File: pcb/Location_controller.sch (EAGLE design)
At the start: 50 parts, among them IC1 LIS302DL

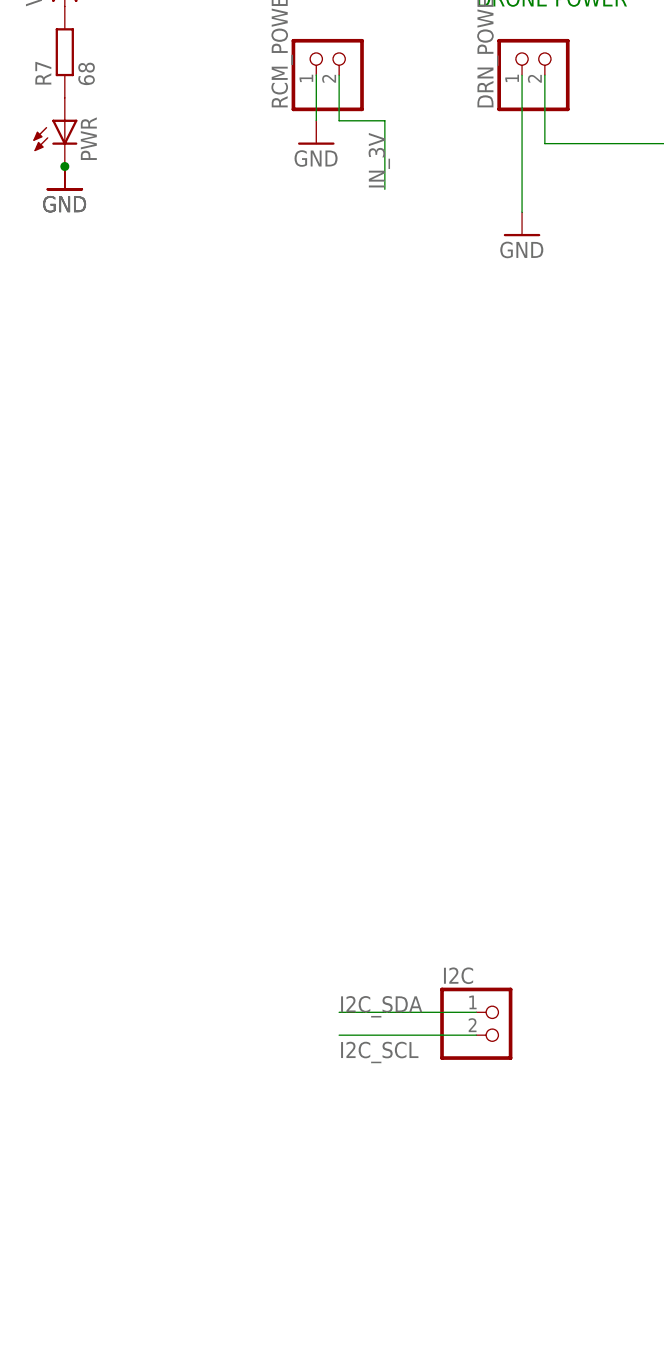
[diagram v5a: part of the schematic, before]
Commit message: Add Zener Diodes to I2C pins
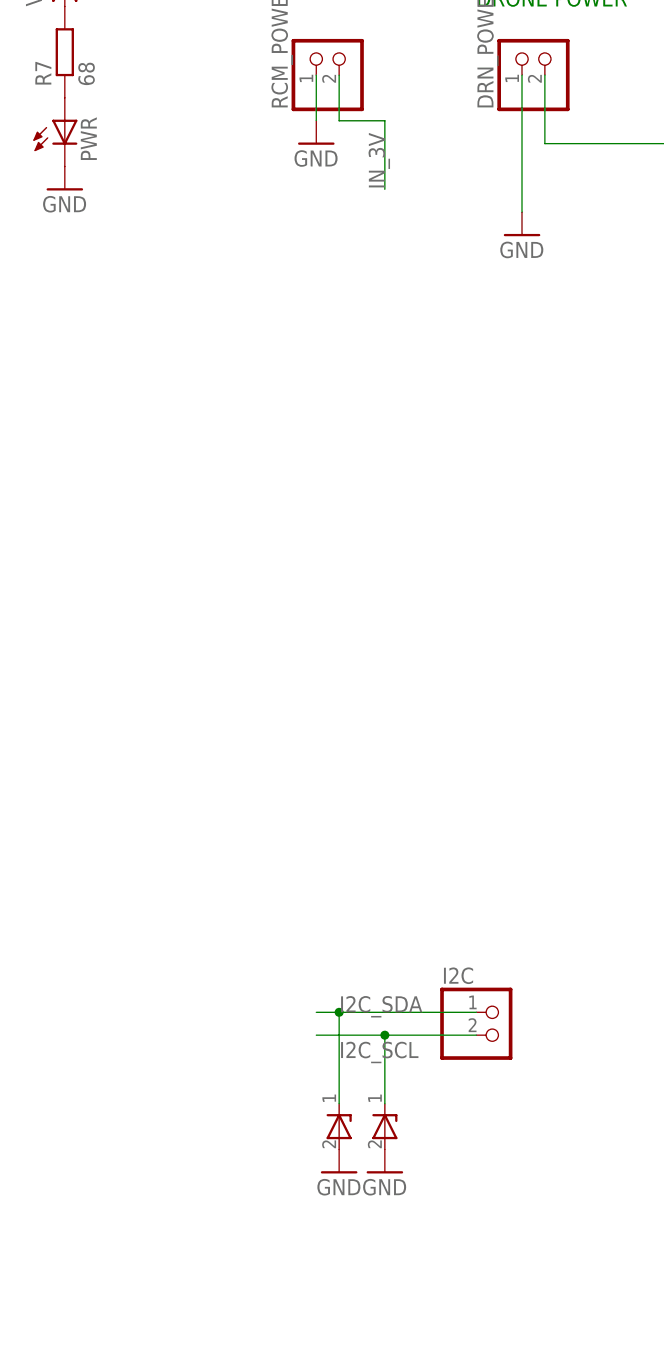
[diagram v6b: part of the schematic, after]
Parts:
- added D1, D2: ZDIODE, stm32f4:ZDIODE
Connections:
- net GND: now also D1.P2, D2.P2
- net I2C_SCL: now also D2.P1
- net I2C_SDA: now also D1.P1
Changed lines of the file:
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@@
 <part name="R8" library="eagle-ltspice" deviceset="R" device="" value="68"/>
 <part name="ERR" library="eagle-ltspice" deviceset="LED_E" device=""/>
-<part name="GND21" library="supply1" deviceset="GND" device=""/>
 <part name="GND22" library="supply1" deviceset="GND" device=""/>
 <part name="I2C" library="pinhead" deviceset="PINHD-1X2" device=""/>
+<part name="D1" library="stm32f4" deviceset="ZDIODE" device=""/>
+<part name="D2" library="stm32f4" deviceset="ZDIODE" device=""/>
+<part name="GND23" library="supply1" deviceset="GND" device=""/>
+<part name="GND24" library="supply1" deviceset="GND" device=""/>
 </parts>
 <sheets>
@@
 <instance part="R8" gate="G$1" x="147.32" y="48.26" rot="R90"/>
 <instance part="ERR" gate="G$1" x="147.32" y="38.1"/>
-<instance part="GND21" gate="1" x="-154.94" y="106.68"/>
 <instance part="GND22" gate="1" x="147.32" y="27.94"/>
 <instance part="I2C" gate="G$1" x="-106.68" y="12.7"/>
+<instance part="D1" gate="G$1" x="-124.46" y="2.54" rot="R90"/>
+<instance part="D2" gate="G$1" x="-119.38" y="2.54" rot="R90"/>
+<instance part="GND23" gate="1" x="-124.46" y="-2.54"/>
+<instance part="GND24" gate="1" x="-119.38" y="-2.54"/>
 </instances>
 <busses>
@@
 <pinref part="PWR" gate="G$1" pin="C"/>
 <pinref part="GND20" gate="1" pin="GND"/>
-<pinref part="GND21" gate="1" pin="GND"/>
-<junction x="-154.94" y="109.22"/>
-<pinref part="GND21" gate="1" pin="GND"/>
 </segment>
 <segment>
@@
 <pinref part="ERR" gate="G$1" pin="C"/>
 <wire x1="147.32" y1="30.48" x2="147.32" y2="33.02" width="0.1524" layer="91"/>
+</segment>
+<segment>
+<pinref part="D1" gate="G$1" pin="P2"/>
+<pinref part="GND23" gate="1" pin="GND"/>
+</segment>
+<segment>
+<pinref part="D2" gate="G$1" pin="P2"/>
+<pinref part="GND24" gate="1" pin="GND"/>
 </segment>
 </net>
@@
 <segment>
 <pinref part="I2C" gate="G$1" pin="2"/>
-<wire x1="-109.22" y1="12.7" x2="-124.46" y2="12.7" width="0.1524" layer="91"/>
+<wire x1="-109.22" y1="12.7" x2="-119.38" y2="12.7" width="0.1524" layer="91"/>
 <label x="-124.46" y="10.16" size="1.778" layer="95"/>
+<pinref part="D2" gate="G$1" pin="P1"/>
+<wire x1="-119.38" y1="12.7" x2="-127" y2="12.7" width="0.1524" layer="91"/>
+<wire x1="-119.38" y1="5.08" x2="-119.38" y2="12.7" width="0.1524" layer="91"/>
+<junction x="-119.38" y="12.7"/>
 </segment>
 </net>
@@
 <wire x1="-109.22" y1="15.24" x2="-124.46" y2="15.24" width="0.1524" layer="91"/>
 <label x="-124.46" y="15.24" size="1.778" layer="95"/>
-</segment>
-</net>
+<pinref part="D1" gate="G$1" pin="P1"/>
+<wire x1="-124.46" y1="15.24" x2="-127" y2="15.24" width="0.1524" layer="91"/>
+<wire x1="-124.46" y1="5.08" x2="-124.46" y2="15.24" width="0.1524" layer="91"/>
+<junction x="-124.46" y="15.24"/>
+</segment>
+</net>

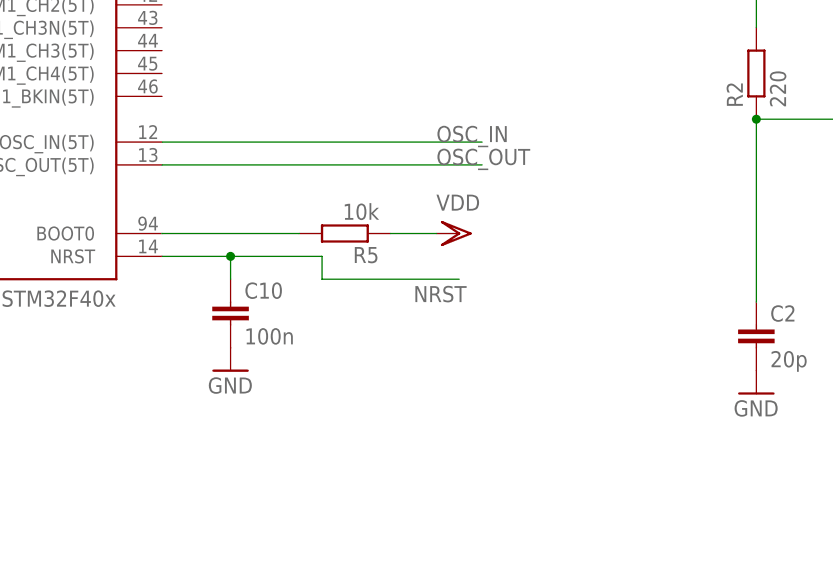
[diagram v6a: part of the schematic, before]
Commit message: Add resistor to GND at BOOT0
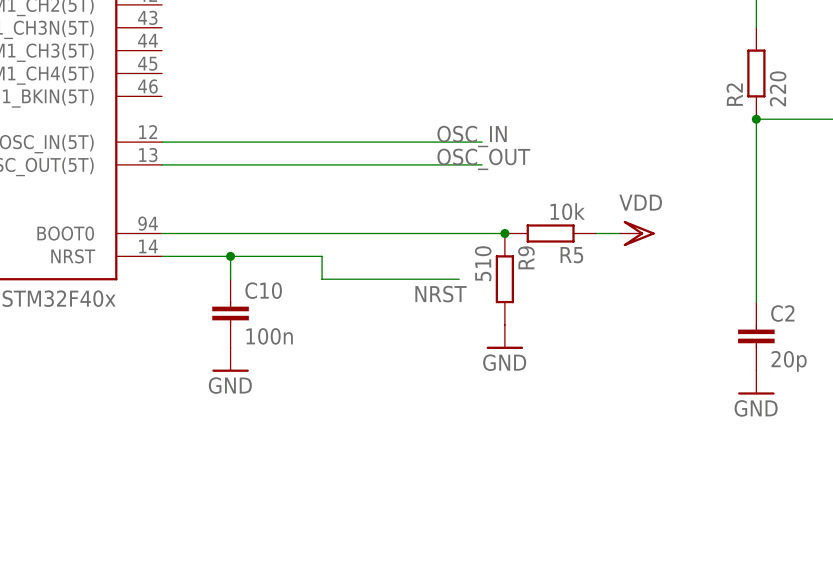
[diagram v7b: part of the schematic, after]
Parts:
- added R9: 510, eagle-ltspice:R
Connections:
- net GND: now also R9.2
- net N$3: now also R9.1
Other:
- moved on the sheet: R5
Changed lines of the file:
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@@
 <part name="GND23" library="supply1" deviceset="GND" device=""/>
 <part name="GND24" library="supply1" deviceset="GND" device=""/>
+<part name="R9" library="eagle-ltspice" deviceset="R" device="" value="510"/>
+<part name="GND21" library="supply1" deviceset="GND" device=""/>
 </parts>
 <sheets>
@@
 <instance part="POWER" gate="A" x="-78.74" y="99.06" rot="R270"/>
 <instance part="GND7" gate="1" x="-40.64" y="-81.28"/>
-<instance part="VDD2" gate="G$1" x="152.4" y="-7.62" rot="R270"/>
-<instance part="R5" gate="G$1" x="139.7" y="-7.62" rot="R180"/>
+<instance part="VDD2" gate="G$1" x="172.72" y="-7.62" rot="R270"/>
+<instance part="R5" gate="G$1" x="162.56" y="-7.62" rot="R180"/>
 <instance part="VDD8" gate="G$1" x="40.64" y="147.32"/>
 <instance part="C26" gate="G$1" x="238.76" y="93.98"/>
@@
 <instance part="GND23" gate="1" x="-124.46" y="-2.54"/>
 <instance part="GND24" gate="1" x="-119.38" y="-2.54"/>
+<instance part="R9" gate="G$1" x="157.48" y="-12.7" rot="R270"/>
+<instance part="GND21" gate="1" x="157.48" y="-20.32"/>
 </instances>
 <busses>
@@
 <pinref part="GND24" gate="1" pin="GND"/>
 </segment>
+<segment>
+<pinref part="R9" gate="G$1" pin="2"/>
+<pinref part="GND21" gate="1" pin="GND"/>
+</segment>
 </net>
 <net name="N$1" class="0">
@@
 </segment>
 <segment>
-<pinref part="R5" gate="G$1" pin="1"/>
-<pinref part="VDD2" gate="G$1" pin="VDD"/>
-<wire x1="144.78" y1="-7.62" x2="149.86" y2="-7.62" width="0.1524" layer="91"/>
-</segment>
-<segment>
 <pinref part="U$1" gate="G$1" pin="VBAT"/>
 <pinref part="VDD8" gate="G$1" pin="VDD"/>
@@
 <pinref part="VDD10" gate="G$1" pin="VDD"/>
 </segment>
+<segment>
+<pinref part="R5" gate="G$1" pin="1"/>
+<pinref part="VDD2" gate="G$1" pin="VDD"/>
+<wire x1="167.64" y1="-7.62" x2="170.18" y2="-7.62" width="0.1524" layer="91"/>
+</segment>
 </net>
 <net name="I2C_SCL" class="0">
@@
 <wire x1="-30.48" y1="-63.5" x2="-30.48" y2="-78.74" width="0.1524" layer="91"/>
 <label x="-30.48" y="-78.74" size="1.778" layer="95" rot="R90"/>
-</segment>
-</net>
-<net name="N$3" class="0">
-<segment>
-<pinref part="R5" gate="G$1" pin="2"/>
-<pinref part="U$1" gate="G$1" pin="BOOT0"/>
-<wire x1="134.62" y1="-7.62" x2="119.38" y2="-7.62" width="0.1524" layer="91"/>
 </segment>
 </net>
@@
 </segment>
 </net>
+<net name="N$3" class="0">
+<segment>
+<pinref part="R5" gate="G$1" pin="2"/>
+<pinref part="R9" gate="G$1" pin="1"/>
+<pinref part="U$1" gate="G$1" pin="BOOT0"/>
+<wire x1="157.48" y1="-7.62" x2="119.38" y2="-7.62" width="0.1524" layer="91"/>
+<junction x="157.48" y="-7.62"/>
+</segment>
+</net>

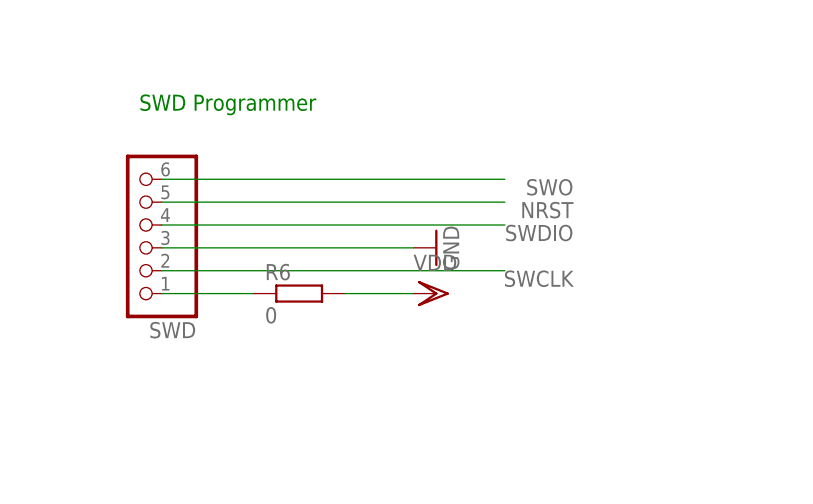
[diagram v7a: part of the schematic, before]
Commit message: added zener to SWDIO EN SWO
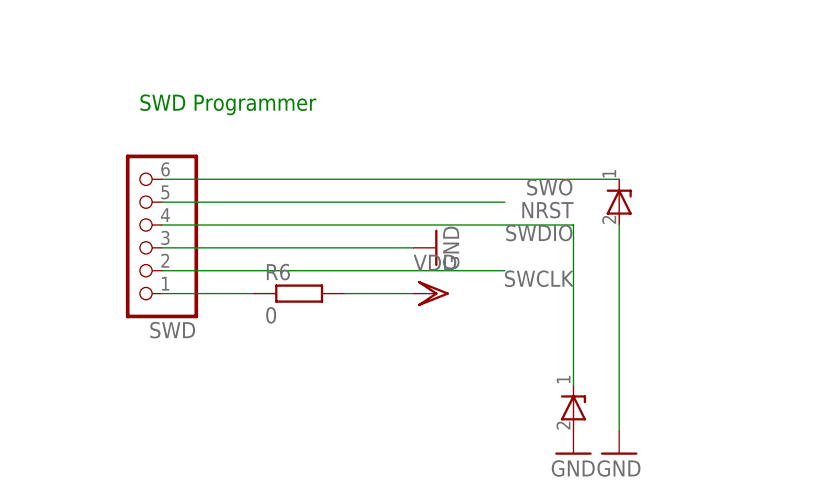
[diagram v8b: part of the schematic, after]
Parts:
- added D3, D4: ZDIODE, stm32f4:ZDIODE
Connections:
- net GND: now also D3.P2, D4.P2
- net SWDIO: now also D4.P1
- net SWO: now also D3.P1
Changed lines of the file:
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@@
 <?xml version="1.0" encoding="utf-8"?>
 <!DOCTYPE eagle SYSTEM "eagle.dtd">
-<eagle version="6.5.0">
+<eagle version="6.4">
 <drawing>
 <settings>
@@
 <part name="R9" library="eagle-ltspice" deviceset="R" device="" value="510"/>
 <part name="GND21" library="supply1" deviceset="GND" device=""/>
+<part name="D4" library="stm32f4" deviceset="ZDIODE" device=""/>
+<part name="GND26" library="supply1" deviceset="GND" device=""/>
+<part name="D3" library="stm32f4" deviceset="ZDIODE" device=""/>
+<part name="GND25" library="supply1" deviceset="GND" device=""/>
 </parts>
 <sheets>
@@
 <instance part="R9" gate="G$1" x="157.48" y="-12.7" rot="R270"/>
 <instance part="GND21" gate="1" x="157.48" y="-20.32"/>
+<instance part="D4" gate="G$1" x="73.66" y="-83.82" rot="R90"/>
+<instance part="GND26" gate="1" x="73.66" y="-88.9"/>
+<instance part="D3" gate="G$1" x="78.74" y="-60.96" rot="R90"/>
+<instance part="GND25" gate="1" x="78.74" y="-88.9"/>
 </instances>
 <busses>
@@
 <pinref part="GND21" gate="1" pin="GND"/>
 </segment>
+<segment>
+<pinref part="D4" gate="G$1" pin="P2"/>
+<pinref part="GND26" gate="1" pin="GND"/>
+</segment>
+<segment>
+<pinref part="D3" gate="G$1" pin="P2"/>
+<pinref part="GND25" gate="1" pin="GND"/>
+<wire x1="78.74" y1="-86.36" x2="78.74" y2="-63.5" width="0.1524" layer="91"/>
+</segment>
 </net>
 <net name="N$1" class="0">
@@
 <segment>
 <pinref part="SWD" gate="A" pin="6"/>
-<wire x1="27.94" y1="-58.42" x2="66.04" y2="-58.42" width="0.1524" layer="91"/>
+<wire x1="27.94" y1="-58.42" x2="78.74" y2="-58.42" width="0.1524" layer="91"/>
 <label x="73.66" y="-58.42" size="1.778" layer="95" rot="R180"/>
+<pinref part="D3" gate="G$1" pin="P1"/>
 </segment>
 <segment>
@@
 <net name="SWDIO" class="0">
 <segment>
-<pinref part="SWD" gate="A" pin="4"/>
-<wire x1="27.94" y1="-63.5" x2="66.04" y2="-63.5" width="0.1524" layer="91"/>
-<label x="73.66" y="-63.5" size="1.778" layer="95" rot="R180"/>
-</segment>
-<segment>
 <pinref part="U$1" gate="G$1" pin="PA13/JTMS-SWDAT(5T)"/>
 <wire x1="40.64" y1="38.1" x2="22.86" y2="38.1" width="0.1524" layer="91"/>
 <label x="22.86" y="38.1" size="1.778" layer="95"/>
 </segment>
-</net>
+<segment>
+<pinref part="SWD" gate="A" pin="4"/>
+<wire x1="27.94" y1="-63.5" x2="73.66" y2="-63.5" width="0.1524" layer="91"/>
+<label x="73.66" y="-63.5" size="1.778" layer="95" rot="R180"/>
+<wire x1="73.66" y1="-63.5" x2="73.66" y2="-81.28" width="0.1524" layer="91"/>
+<pinref part="D4" gate="G$1" pin="P1"/>
+</segment>
+</net>
